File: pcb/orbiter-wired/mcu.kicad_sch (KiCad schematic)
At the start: 24 parts, among them J4 AudioJack4, Q2 BSS138, SW28 SW_SPDT

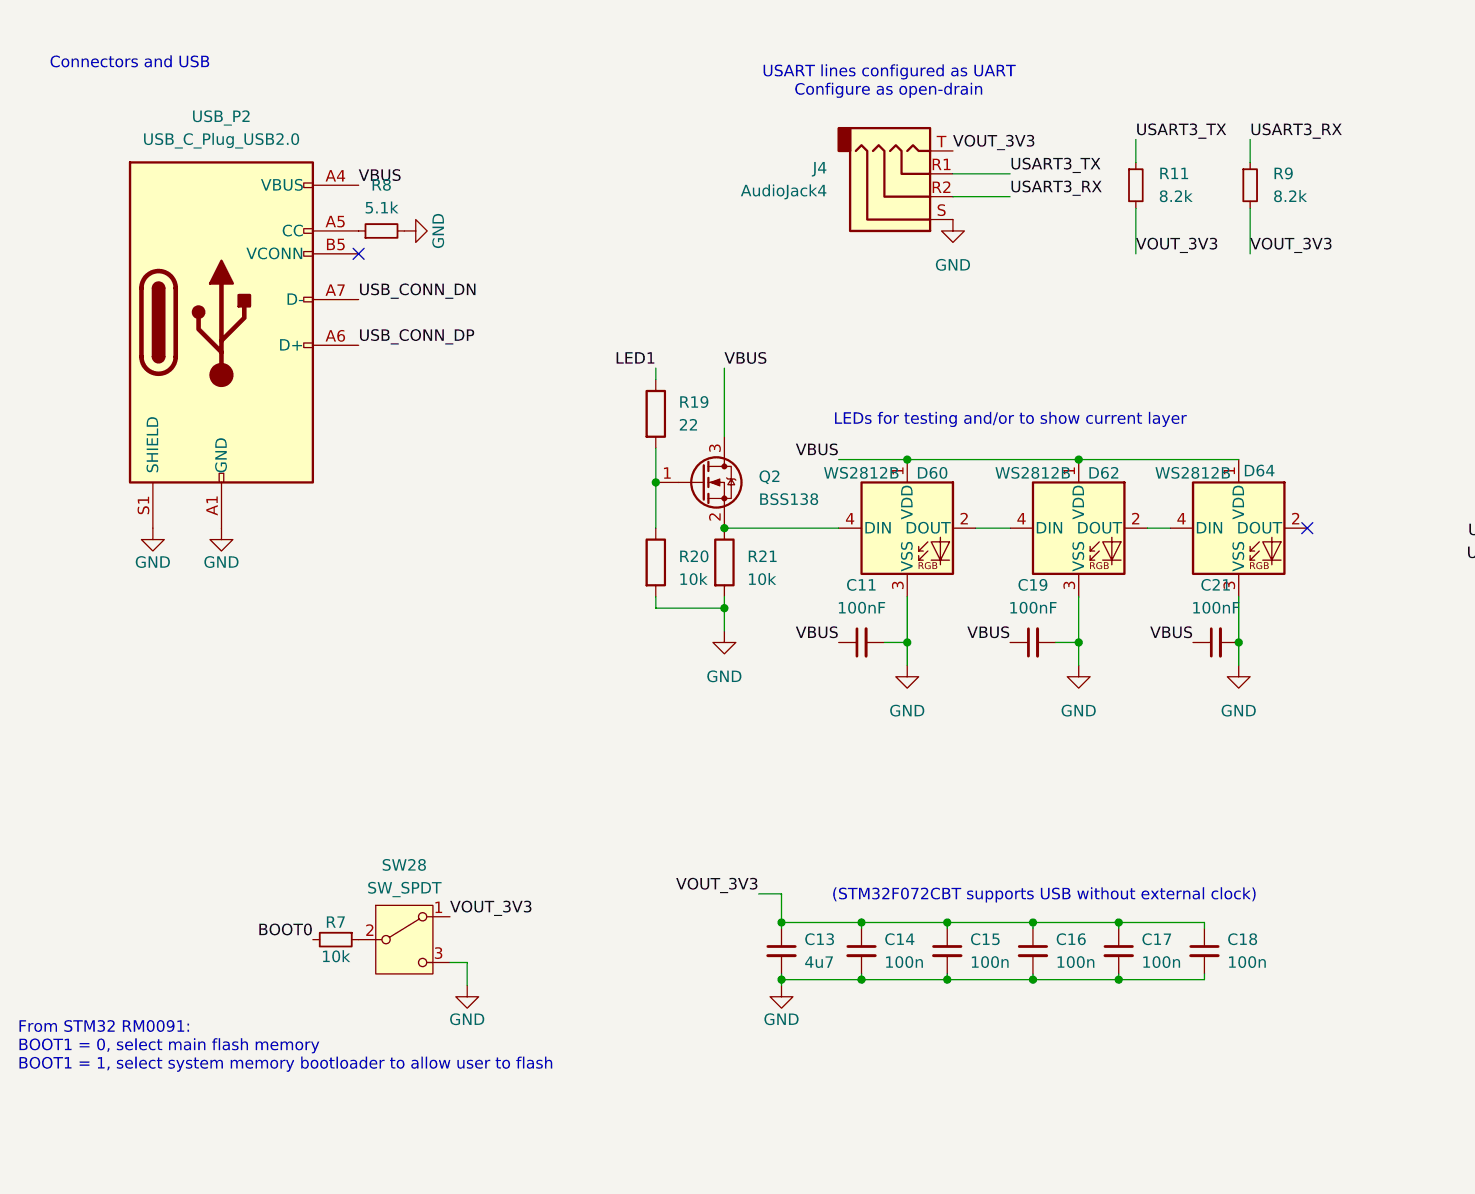
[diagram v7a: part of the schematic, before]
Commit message: Edit project files to prepare for manufacturing
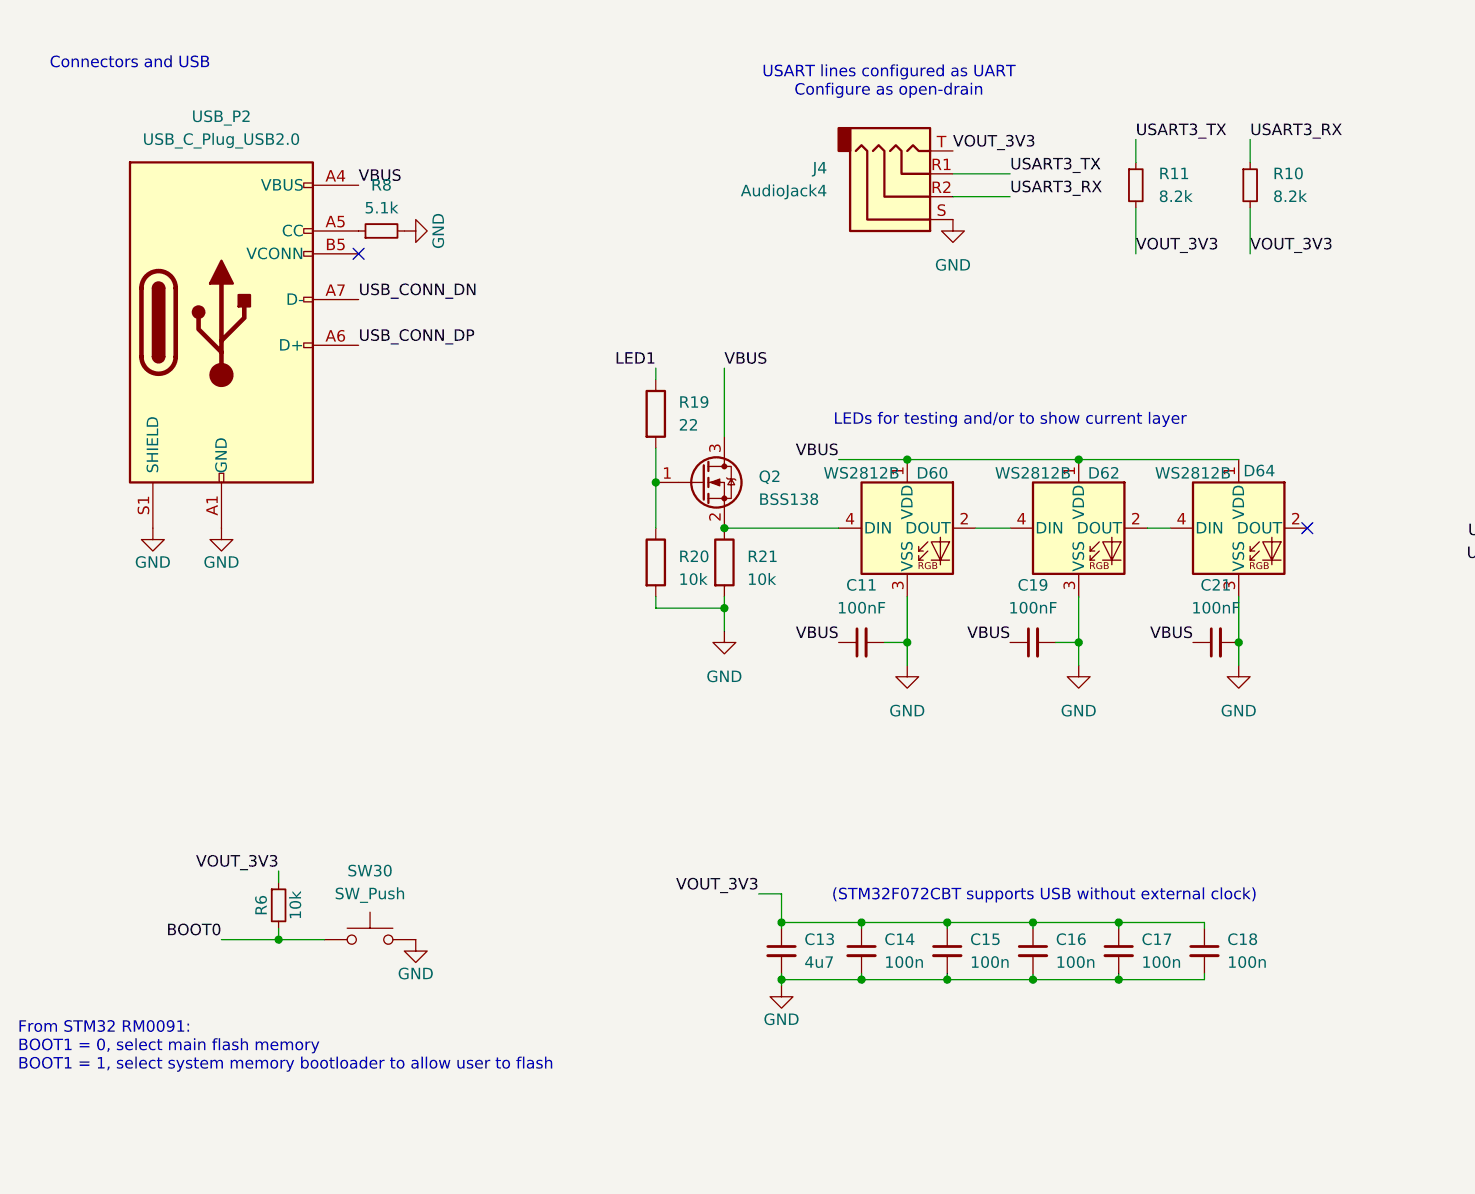
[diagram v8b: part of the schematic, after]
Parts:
- removed R7: 10k, Resistor_SMD:R_0603_1608Metric, symbol Device:R_Small
- removed SW28: SW_SPDT, Button_Switch_SMD:SW_SPST_PTS647_Sx38, symbol Switch:SW_SPDT
- added R6: 10k, Resistor_SMD:R_0603_1608Metric, symbol Device:R_Small
- added SW30: SW_Push, Button_Switch_SMD:SW_SPST_PTS647_Sx38, symbol Switch:SW_Push
- renumbered R9 to R10
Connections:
- net BOOT0: now also R6.2, SW30.1
- net GND: now also SW30.2
- net VOUT_3V3: now also R6.1
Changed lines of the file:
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@@
 	)
 	(junction
+		(at 58.42 123.19)
+		(diameter 0)
+		(color 0 0 0 0)
+	)
+	(junction
 		(at 114.3 121.285)
 		(diameter 0)
@@
 	(wire
 		(pts
+			(xy 52.07 123.19) (xy 58.42 123.19)
+		)
+		(stroke
+			(width 0)
+			(type default)
+		)
+	)
+	(wire
+		(pts
 			(xy 144.78 90.17) (xy 147.32 90.17)
 		)
@@
 	(wire
 		(pts
+			(xy 58.42 123.19) (xy 63.5 123.19)
+		)
+		(stroke
+			(width 0)
+			(type default)
+		)
+	)
+	(wire
+		(pts
 			(xy 251.46 87.63) (xy 260.35 87.63)
 		)
@@
 		)
 	)
+	(wire
+		(pts
+			(xy 58.42 121.92) (xy 58.42 123.19)
+		)
+		(stroke
+			(width 0)
+			(type default)
+		)
+	)
 	(bus
 		(pts
@@
 	(wire
 		(pts
-			(xy 79.375 125.73) (xy 77.47 125.73)
+			(xy 58.42 116.84) (xy 58.42 115.57)
 		)
 		(stroke
@@
 	(wire
 		(pts
-			(xy 79.375 128.27) (xy 79.375 125.73)
-		)
-		(stroke
-			(width 0)
-			(type default)
-		)
-	)
-	(wire
-		(pts
 			(xy 218.44 99.06) (xy 215.9 99.06)
 		)
@@
 		)
 	)
+	(label "BOOT0"
+		(at 52.07 123.19 180)
+		(fields_autoplaced yes)
+		(effects
+			(font
+				(size 1.27 1.27)
+			)
+			(justify right bottom)
+		)
+	)
 	(label "NRST"
 		(at 200.66 25.4 180)
@@
 		)
 	)
-	(label "VOUT_3V3"
-		(at 77.47 120.65 0)
-		(fields_autoplaced yes)
-		(effects
-			(font
-				(size 1.27 1.27)
-			)
-			(justify left bottom)
-		)
-	)
 	(label "USART3_RX"
 		(at 166.37 34.29 0)
@@
 		)
 	)
+	(label "VOUT_3V3"
+		(at 58.42 115.57 180)
+		(fields_autoplaced yes)
+		(effects
+			(font
+				(size 1.27 1.27)
+			)
+			(justify right bottom)
+		)
+	)
 	(label "NRST"
 		(at 251.46 118.11 180)
@@
 		)
 	)
-	(label "BOOT0"
-		(at 62.23 123.19 180)
-		(fields_autoplaced yes)
-		(effects
-			(font
-				(size 1.27 1.27)
-			)
-			(justify right bottom)
-		)
-	)
 	(label "COL1"
 		(at 246.38 40.64 180)
@@
 	)
 	(symbol
+		(lib_id "Switch:SW_Push")
+		(at 68.58 123.19 0)
+		(unit 1)
+		(exclude_from_sim no)
+		(in_bom yes)
+		(on_board yes)
+		(dnp no)
+		(fields_autoplaced yes)
+		(property "Reference" "SW30"
+			(at 68.58 115.57 0)
+			(effects
+				(font
+					(size 1.27 1.27)
+				)
+			)
+		)
+		(property "Value" "SW_Push"
+			(at 68.58 118.11 0)
+			(effects
+				(font
+					(size 1.27 1.27)
+				)
+			)
+		)
+		(property "Footprint" "Button_Switch_SMD:SW_SPST_PTS647_Sx38"
+			(at 68.58 118.11 0)
+			(effects
+				(font
+					(size 1.27 1.27)
+				)
+				(hide yes)
+			)
+		)
+		(property "Datasheet" "~"
+			(at 68.58 118.11 0)
+			(effects
+				(font
+					(size 1.27 1.27)
+				)
+				(hide yes)
+			)
+		)
+		(property "Description" "Push button switch, generic, two pins"
+			(at 68.58 123.19 0)
+			(effects
+				(font
+					(size 1.27 1.27)
+				)
+				(hide yes)
+			)
+		)
+		(pin "2"
+		)
+		(pin "1"
+		)
+		(instances
+			(project ""
+				(path "/623f70b3-6381-43ff-98c1-e36c34bee313/c14a50ad-c630-40dd-ac14-b3b40c9c245d"
+					(reference "SW30")
+					(unit 1)
+				)
+				(path "/623f70b3-6381-43ff-98c1-e36c34bee313/e058b5b4-db4d-4bc7-8f42-8e3bd37c89bf"
+					(reference "SW29")
+					(unit 1)
+				)
+			)
+		)
+	)
+	(symbol
 		(lib_id "STM32F4_REV2-rescue:GND-power")
 		(at 52.07 77.47 0)
@@
 	)
 	(symbol
+		(lib_id "Device:R_Small")
+		(at 58.42 119.38 0)
+		(unit 1)
+		(exclude_from_sim no)
+		(in_bom yes)
+		(on_board yes)
+		(dnp no)
+		(property "Reference" "R6"
+			(at 56.515 119.38 90)
+			(effects
+				(font
+					(size 1.27 1.27)
+				)
+			)
+		)
+		(property "Value" "10k"
+			(at 60.325 119.38 90)
+			(effects
+				(font
+					(size 1.27 1.27)
+				)
+			)
+		)
+		(property "Footprint" "Resistor_SMD:R_0603_1608Metric"
+			(at 58.42 119.38 0)
+			(effects
+				(font
+					(size 1.27 1.27)
+				)
+				(hide yes)
+			)
+		)
+		(property "Datasheet" "~"
+			(at 58.42 119.38 0)
+			(effects
+				(font
+					(size 1.27 1.27)
+				)
+				(hide yes)
+			)
+		)
+		(property "Description" ""
+			(at 58.42 119.38 0)
+			(effects
+				(font
+					(size 1.27 1.27)
+				)
+				(hide yes)
+			)
+		)
+		(pin "1"
+		)
+		(pin "2"
+		)
+		(instances
+			(project "orbiter"
+				(path "/623f70b3-6381-43ff-98c1-e36c34bee313/c14a50ad-c630-40dd-ac14-b3b40c9c245d"
+					(reference "R7")
+					(unit 1)
+				)
+				(path "/623f70b3-6381-43ff-98c1-e36c34bee313/e058b5b4-db4d-4bc7-8f42-8e3bd37c89bf"
+					(reference "R6")
+					(unit 1)
+				)
+			)
+		)
+	)
+	(symbol
 		(lib_id "LED:WS2812B")
 		(at 147.32 77.47 0)
@@
 	(symbol
 		(lib_id "STM32F4_REV2-rescue:GND-power")
-		(at 79.375 128.27 0)
+		(at 73.66 123.19 0)
 		(unit 1)
 		(exclude_from_sim no)
@@
 		(on_board yes)
 		(dnp no)
-		(property "Reference" "#PWR018"
-			(at 79.375 134.62 0)
+		(property "Reference" "#PWR012"
+			(at 73.66 129.54 0)
 			(effects
 				(font
@@
 		)
 		(property "Value" "GND"
-			(at 79.375 132.08 0)
+			(at 73.66 127 0)
 			(effects
 				(font
@@
 		)
 		(property "Footprint" ""
-			(at 79.375 128.27 0)
+			(at 73.66 123.19 0)
 			(effects
 				(font
@@
 		)
 		(property "Datasheet" ""
-			(at 79.375 128.27 0)
+			(at 73.66 123.19 0)
 			(effects
 				(font
@@
 		)
 		(property "Description" ""
-			(at 79.375 128.27 0)
+			(at 73.66 123.19 0)
 			(effects
 				(font
@@
 		(dnp no)
 		(fields_autoplaced yes)
-		(property "Reference" "R9"
+		(property "Reference" "R10"
 			(at 168.91 38.0999 0)
 			(effects
@@
 	)
 	(symbol
-		(lib_id "Device:R_Small")
-		(at 64.77 123.19 270)
-		(unit 1)
-		(exclude_from_sim no)
-		(in_bom yes)
-		(on_board yes)
-		(dnp no)
-		(property "Reference" "R7"
-			(at 64.77 121.285 90)
-			(effects
-				(font
-					(size 1.27 1.27)
-				)
-			)
-		)
-		(property "Value" "10k"
-			(at 64.77 125.095 90)
-			(effects
-				(font
-					(size 1.27 1.27)
-				)
-			)
-		)
-		(property "Footprint" "Resistor_SMD:R_0603_1608Metric"
-			(at 64.77 123.19 0)
-			(effects
-				(font
-					(size 1.27 1.27)
-				)
-				(hide yes)
-			)
-		)
-		(property "Datasheet" "~"
-			(at 64.77 123.19 0)
-			(effects
-				(font
-					(size 1.27 1.27)
-				)
-				(hide yes)
-			)
-		)
-		(property "Description" ""
-			(at 64.77 123.19 0)
-			(effects
-				(font
-					(size 1.27 1.27)
-				)
-				(hide yes)
-			)
-		)
-		(pin "1"
-		)
-		(pin "2"
-		)
-		(instances
-			(project "orbiter"
-				(path "/623f70b3-6381-43ff-98c1-e36c34bee313/c14a50ad-c630-40dd-ac14-b3b40c9c245d"
-					(reference "R7")
-					(unit 1)
-				)
-				(path "/623f70b3-6381-43ff-98c1-e36c34bee313/e058b5b4-db4d-4bc7-8f42-8e3bd37c89bf"
-					(reference "R6")
-					(unit 1)
-				)
-			)
-		)
-	)
-	(symbol
 		(lib_id "LED:WS2812B")
 		(at 165.1 77.47 0)
@@
 					(unit 1)
 				)
-			)
-		)
-	)
-	(symbol
-		(lib_id "Switch:SW_SPDT")
-		(at 72.39 123.19 0)
-		(unit 1)
-		(exclude_from_sim no)
-		(in_bom yes)
-		(on_board yes)
-		(dnp no)
-		(property "Reference" "SW28"
-			(at 72.39 114.935 0)
-			(effects
-				(font
-					(size 1.27 1.27)
-				)
-			)
-		)
-		(property "Value" "SW_SPDT"
-			(at 72.39 117.475 0)
-			(effects
-				(font
-					(size 1.27 1.27)
-				)
-			)
-		)
-		(property "Footprint" "Button_Switch_SMD:SW_SPST_PTS647_Sx38"
-			(at 72.39 123.19 0)
-			(effects
-				(font
-					(size 1.27 1.27)
-				)
-				(hide yes)
-			)
-		)
-		(property "Datasheet" "~"
-			(at 72.39 123.19 0)
-			(effects
-				(font
-					(size 1.27 1.27)
-				)
-				(hide yes)
-			)
-		)
-		(property "Description" ""
-			(at 72.39 123.19 0)
-			(effects
-				(font
-					(size 1.27 1.27)
-				)
-				(hide yes)
-			)
-		)
-		(pin "1"
-		)
-		(pin "2"
-		)
-		(pin "3"
-		)
-		(instances
-			(project "orbiter"
-				(path "/623f70b3-6381-43ff-98c1-e36c34bee313/c14a50ad-c630-40dd-ac14-b3b40c9c245d"
-					(reference "SW28")
-					(unit 1)
-				)
-				(path "/623f70b3-6381-43ff-98c1-e36c34bee313/e058b5b4-db4d-4bc7-8f42-8e3bd37c89bf"
-					(reference "SW1")
-					(unit 1)
-				)
